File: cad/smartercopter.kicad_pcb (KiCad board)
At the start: 2 copper layers, 37.7 x 16.8 mm, 74 parts, among them P1 CONN_5, P2 CONN_01X01, P3 CONN_01X01, P4 CONN_2, P5 CONN_01X01, P6 CONN_01X01, P7 CONN_01X01, Q1 SiA910EDJ, SW1 SW_PUSH_4, U1 CC2541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

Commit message: everything on board
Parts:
- C1, C2, C3, C6, C7, C8, P1: moved to B.Cu
- moved C25 29.3 mm to (69.7, 119.7), turned to 90 degrees
- moved R11 28.5 mm to (75.0, 120.1), turned to 0 degrees
- moved C27 28.1 mm to (69.6, 118.8), turned to 90 degrees
- moved R18 27.9 mm to (70.8, 119.0), turned to 90 degrees
- moved C21 27.5 mm to (73.6, 119.3), turned to 90 degrees
- moved C17 27.2 mm to (75.5, 119.3), turned to 90 degrees
- moved R19 26.8 mm to (69.7, 117.9), turned to 90 degrees
- moved U4 26.8 mm to (72.1, 118.5), turned to 90 degrees
- moved C18 26.2 mm to (75.1, 118.5), turned to 180 degrees
- moved C23 25.2 mm to (70.2, 116.8), turned to 180 degrees
- moved R15 23.8 mm to (70.2, 115.8), turned to 0 degrees
- moved P1 14.0 mm to (75.3, 107.4), turned to 180 degrees
- moved R16 11.7 mm to (65.1, 108.1)
- moved U3 11.7 mm to (65.6, 108.2)
- moved C20 11.7 mm to (65.1, 109.5)
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
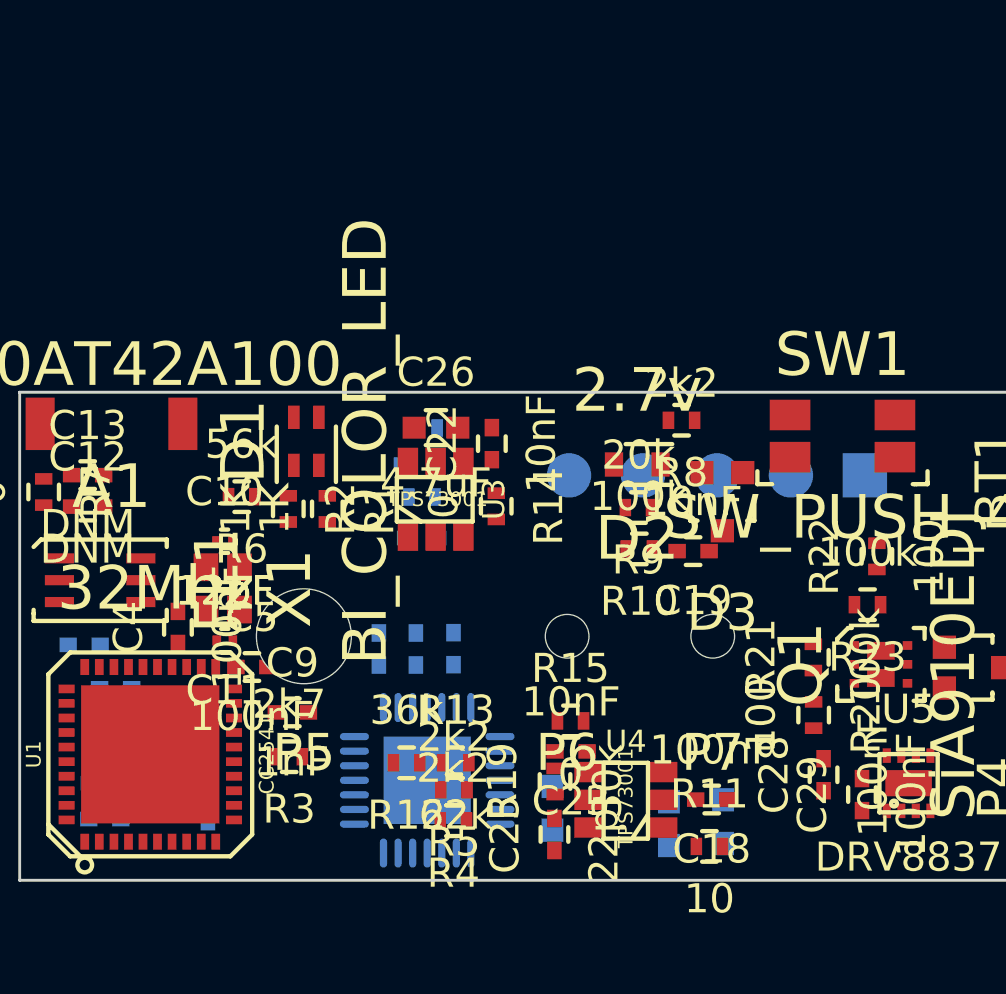
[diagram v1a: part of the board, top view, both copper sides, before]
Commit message: routing first, then placing
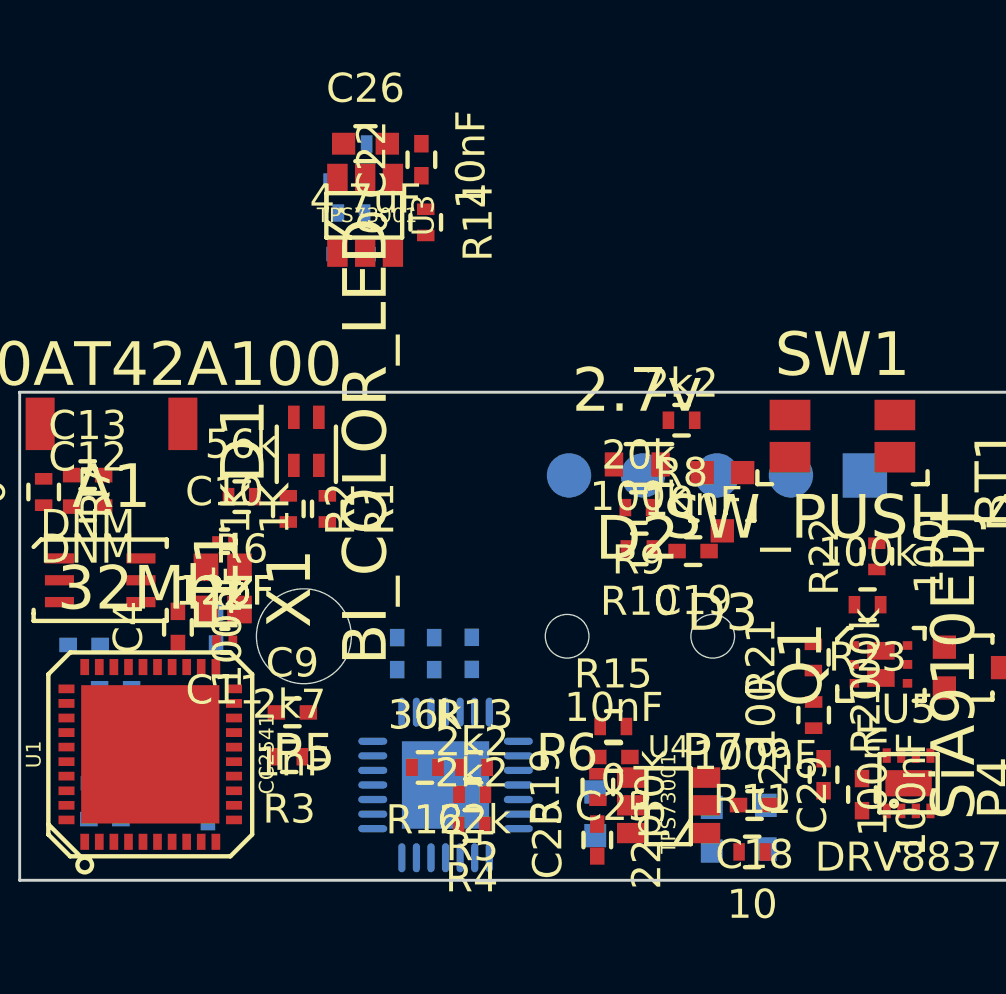
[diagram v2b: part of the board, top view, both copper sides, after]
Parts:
- C5: moved to B.Cu
- moved C20 10.0 mm to (62.7, 99.8)
- moved C22 10.0 mm to (65.1, 96.5)
- moved C24 10.0 mm to (62.6, 97.2)
- moved C26 10.0 mm to (63.2, 96.0)
- moved R14 10.0 mm to (65.3, 98.7)
- moved R16 10.0 mm to (62.7, 98.4)
- moved R17 10.0 mm to (63.7, 96.0)
- moved U3 10.0 mm to (63.2, 98.4)
- moved C5 1.82 mm to (58.1, 112.6), turned to 90 degrees
- moved C23 1.48 mm to (71.7, 117.0)
- moved C17 1.48 mm to (76.9, 119.5)
- moved C18 1.48 mm to (76.5, 118.7)
- moved C21 1.48 mm to (75.1, 119.5)
- moved C25 1.48 mm to (71.2, 119.9)
- moved C27 1.48 mm to (71.1, 119.0)
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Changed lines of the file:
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@@
     (links 168)
     (no_connects 168)
-    (area 39.758145 90.69 93.643934 123.148092)
+    (area 39.758145 101.697 93.643934 123.148092)
     (thickness 1.6)
     (drawings 6)
@@
     )
   )
-  (module Capacitors_SMD:C_0402 (layer F.Cu)
-    (at 59.29 113.95)
-    (descr "Capacitor SMD 0402, reflow soldering, AVX (see smccp.pdf)")
-    (tags "capacitor 0402")
-    (attr smd)
-    (fp_text reference C5 (at 0 -1.7) (layer F.SilkS)
-      (effects (font (size 1 1) (thickness 0.15)))
-    )
-    (fp_text value 100nF (at 0 1.7) (layer F.SilkS)
-      (effects (font (size 1 1) (thickness 0.15)))
-    )
-    (fp_line (start -1.15 -0.6) (end 1.15 -0.6) (layer F.CrtYd) (width 0.05))
-    (fp_line (start -1.15 0.6) (end 1.15 0.6) (layer F.CrtYd) (width 0.05))
-    (fp_line (start -1.15 -0.6) (end -1.15 0.6) (layer F.CrtYd) (width 0.05))
-    (fp_line (start 1.15 -0.6) (end 1.15 0.6) (layer F.CrtYd) (width 0.05))
-    (fp_line (start 0.25 -0.475) (end -0.25 -0.475) (layer F.SilkS) (width 0.15))
-    (fp_line (start -0.25 0.475) (end 0.25 0.475) (layer F.SilkS) (width 0.15))
-    (pad 1 smd rect (at -0.55 0) (size 0.6 0.5) (layers F.Cu F.Paste F.Mask)
-      (net 12 VCCA))
-    (pad 2 smd rect (at 0.55 0) (size 0.6 0.5) (layers F.Cu F.Paste F.Mask)
+  (module Capacitors_SMD:C_0402 (layer B.Cu)
+    (at 58.06 112.61 90)
+    (descr "Capacitor SMD 0402, reflow soldering, AVX (see smccp.pdf)")
+    (tags "capacitor 0402")
+    (attr smd)
+    (fp_text reference C5 (at 0 1.7 90) (layer B.SilkS)
+      (effects (font (size 1 1) (thickness 0.15)) (justify mirror))
+    )
+    (fp_text value 100nF (at 0 -1.7 90) (layer B.SilkS)
+      (effects (font (size 1 1) (thickness 0.15)) (justify mirror))
+    )
+    (fp_line (start -1.15 0.6) (end 1.15 0.6) (layer B.CrtYd) (width 0.05))
+    (fp_line (start -1.15 -0.6) (end 1.15 -0.6) (layer B.CrtYd) (width 0.05))
+    (fp_line (start -1.15 0.6) (end -1.15 -0.6) (layer B.CrtYd) (width 0.05))
+    (fp_line (start 1.15 0.6) (end 1.15 -0.6) (layer B.CrtYd) (width 0.05))
+    (fp_line (start 0.25 0.475) (end -0.25 0.475) (layer B.SilkS) (width 0.15))
+    (fp_line (start -0.25 -0.475) (end 0.25 -0.475) (layer B.SilkS) (width 0.15))
+    (pad 1 smd rect (at -0.55 0 90) (size 0.6 0.5) (layers B.Cu B.Paste B.Mask)
+      (net 12 VCCA))
+    (pad 2 smd rect (at 0.55 0 90) (size 0.6 0.5) (layers B.Cu B.Paste B.Mask)
       (net 5 AGND))
     (model Capacitors_SMD/C_0402E.wrl
@@
   )
   (module Capacitors_SMD:C_0402 (layer B.Cu)
-    (at 64.92 113.33 90)
+    (at 65.55 113.49 90)
     (descr "Capacitor SMD 0402, reflow soldering, AVX (see smccp.pdf)")
     (tags "capacitor 0402")
@@
   )
   (module Capacitors_SMD:C_0402 (layer B.Cu)
-    (at 66.21 113.32 90)
+    (at 66.84 113.48 90)
     (descr "Capacitor SMD 0402, reflow soldering, AVX (see smccp.pdf)")
     (tags "capacitor 0402")
@@
   )
   (module Capacitors_SMD:C_0402 (layer B.Cu)
-    (at 63.65 113.33 90)
+    (at 64.28 113.49 90)
     (descr "Capacitor SMD 0402, reflow soldering, AVX (see smccp.pdf)")
     (tags "capacitor 0402")
@@
   )
   (module Capacitors_SMD:C_0603 (layer B.Cu)
-    (at 75.47 119.26 90)
+    (at 76.94 119.45 90)
     (descr "Capacitor SMD 0603, reflow soldering, AVX (see smccp.pdf)")
     (tags "capacitor 0603")
@@
   )
   (module Capacitors_SMD:C_0402 (layer F.Cu)
-    (at 75.08 118.5 180)
+    (at 76.55 118.69 180)
     (descr "Capacitor SMD 0402, reflow soldering, AVX (see smccp.pdf)")
     (tags "capacitor 0402")
@@
   )
   (module Capacitors_SMD:C_0402 (layer B.Cu)
-    (at 65.12 109.52)
+    (at 62.7 99.77)
     (descr "Capacitor SMD 0402, reflow soldering, AVX (see smccp.pdf)")
     (tags "capacitor 0402")
@@
   )
   (module Capacitors_SMD:C_0603 (layer B.Cu)
-    (at 73.61 119.33 90)
+    (at 75.08 119.52 90)
     (descr "Capacitor SMD 0603, reflow soldering, AVX (see smccp.pdf)")
     (tags "capacitor 0603")
@@
   )
   (module Capacitors_SMD:C_0402 (layer F.Cu)
-    (at 67.53 106.28 90)
+    (at 65.11 96.53 90)
     (descr "Capacitor SMD 0402, reflow soldering, AVX (see smccp.pdf)")
     (tags "capacitor 0402")
@@
   )
   (module Capacitors_SMD:C_0402 (layer F.Cu)
-    (at 70.25 116.85 180)
+    (at 71.72 117.04 180)
     (descr "Capacitor SMD 0402, reflow soldering, AVX (see smccp.pdf)")
     (tags "capacitor 0402")
@@
   )
   (module Capacitors_SMD:C_0402 (layer B.Cu)
-    (at 65.01 107)
+    (at 62.59 97.25)
     (descr "Capacitor SMD 0402, reflow soldering, AVX (see smccp.pdf)")
     (tags "capacitor 0402")
@@
   )
   (module Capacitors_SMD:C_0402 (layer F.Cu)
-    (at 69.68 119.7 90)
+    (at 71.15 119.89 90)
     (descr "Capacitor SMD 0402, reflow soldering, AVX (see smccp.pdf)")
     (tags "capacitor 0402")
@@
   )
   (module Capacitors_SMD:C_0603 (layer F.Cu)
-    (at 65.61 105.73)
+    (at 63.19 95.98)
     (descr "Capacitor SMD 0603, reflow soldering, AVX (see smccp.pdf)")
     (tags "capacitor 0603")
@@
   )
   (module Capacitors_SMD:C_0603 (layer B.Cu)
-    (at 69.61 118.8 90)
+    (at 71.08 118.99 90)
     (descr "Capacitor SMD 0603, reflow soldering, AVX (see smccp.pdf)")
     (tags "capacitor 0603")
@@
   )
   (module Resistors_SMD:R_0402 (layer F.Cu)
-    (at 66.21 119.23 180)
+    (at 66.84 119.39 180)
     (descr "Resistor SMD 0402, reflow soldering, Vishay (see dcrcw.pdf)")
     (tags "resistor 0402")
@@
   )
   (module Resistors_SMD:R_0402 (layer F.Cu)
-    (at 66.228992 118.16156 180)
+    (at 66.858992 118.32156 180)
     (descr "Resistor SMD 0402, reflow soldering, Vishay (see dcrcw.pdf)")
     (tags "resistor 0402")
@@
   )
   (module Resistors_SMD:R_0402 (layer F.Cu)
-    (at 75 120.11)
+    (at 76.47 120.3)
     (descr "Resistor SMD 0402, reflow soldering, Vishay (see dcrcw.pdf)")
     (tags "resistor 0402")
@@
   )
   (module Resistors_SMD:R_0402 (layer F.Cu)
-    (at 64.60159 117.238654 180)
+    (at 65.23159 117.398654 180)
     (descr "Resistor SMD 0402, reflow soldering, Vishay (see dcrcw.pdf)")
     (tags "resistor 0402")
@@
   )
   (module Resistors_SMD:R_0402 (layer F.Cu)
-    (at 66.29 117.23647)
+    (at 66.92 117.39647)
     (descr "Resistor SMD 0402, reflow soldering, Vishay (see dcrcw.pdf)")
     (tags "resistor 0402")
@@
   )
   (module Resistors_SMD:R_0402 (layer F.Cu)
-    (at 67.68 108.43 270)
+    (at 65.26 98.68 270)
     (descr "Resistor SMD 0402, reflow soldering, Vishay (see dcrcw.pdf)")
     (tags "resistor 0402")
@@
   )
   (module Resistors_SMD:R_0402 (layer F.Cu)
-    (at 70.23 115.8)
+    (at 71.7 115.99)
     (descr "Resistor SMD 0402, reflow soldering, Vishay (see dcrcw.pdf)")
     (tags "resistor 0402")
@@
   )
   (module Resistors_SMD:R_0402 (layer B.Cu)
-    (at 65.13 108.11)
+    (at 62.71 98.36)
     (descr "Resistor SMD 0402, reflow soldering, Vishay (see dcrcw.pdf)")
     (tags "resistor 0402")
@@
   )
   (module Resistors_SMD:R_0402 (layer B.Cu)
-    (at 66.1 105.74)
+    (at 63.68 95.99)
     (descr "Resistor SMD 0402, reflow soldering, Vishay (see dcrcw.pdf)")
     (tags "resistor 0402")
@@
   )
   (module Resistors_SMD:R_0402 (layer B.Cu)
-    (at 70.81 119.01 90)
+    (at 72.28 119.2 90)
     (descr "Resistor SMD 0402, reflow soldering, Vishay (see dcrcw.pdf)")
     (tags "resistor 0402")
@@
   )
   (module Resistors_SMD:R_0402 (layer F.Cu)
-    (at 69.7 117.88 90)
+    (at 71.17 118.07 90)
     (descr "Resistor SMD 0402, reflow soldering, Vishay (see dcrcw.pdf)")
     (tags "resistor 0402")
@@
   )
   (module SMD_Packages:QFN-28-1EP (layer B.Cu)
-    (at 65.31 117.84)
+    (at 65.94 118)
     (fp_text reference U2 (at 0 4.20116) (layer B.SilkS)
       (effects (font (size 1.00076 1.00076) (thickness 0.3048)) (justify mirror))
@@
   )
   (module SMD_Packages:SOT-23-6 (layer F.Cu)
-    (at 65.6 108.19)
+    (at 63.18 98.44)
     (fp_text reference U3 (at 1.99898 0 90) (layer F.SilkS)
       (effects (font (size 0.762 0.762) (thickness 0.0762)))
@@
   )
   (module SMD_Packages:SOT-23-6 (layer F.Cu)
-    (at 72.13 118.51 90)
+    (at 73.6 118.7 90)
     (fp_text reference U4 (at 1.99898 0 180) (layer F.SilkS)
       (effects (font (size 0.762 0.762) (thickness 0.0762)))

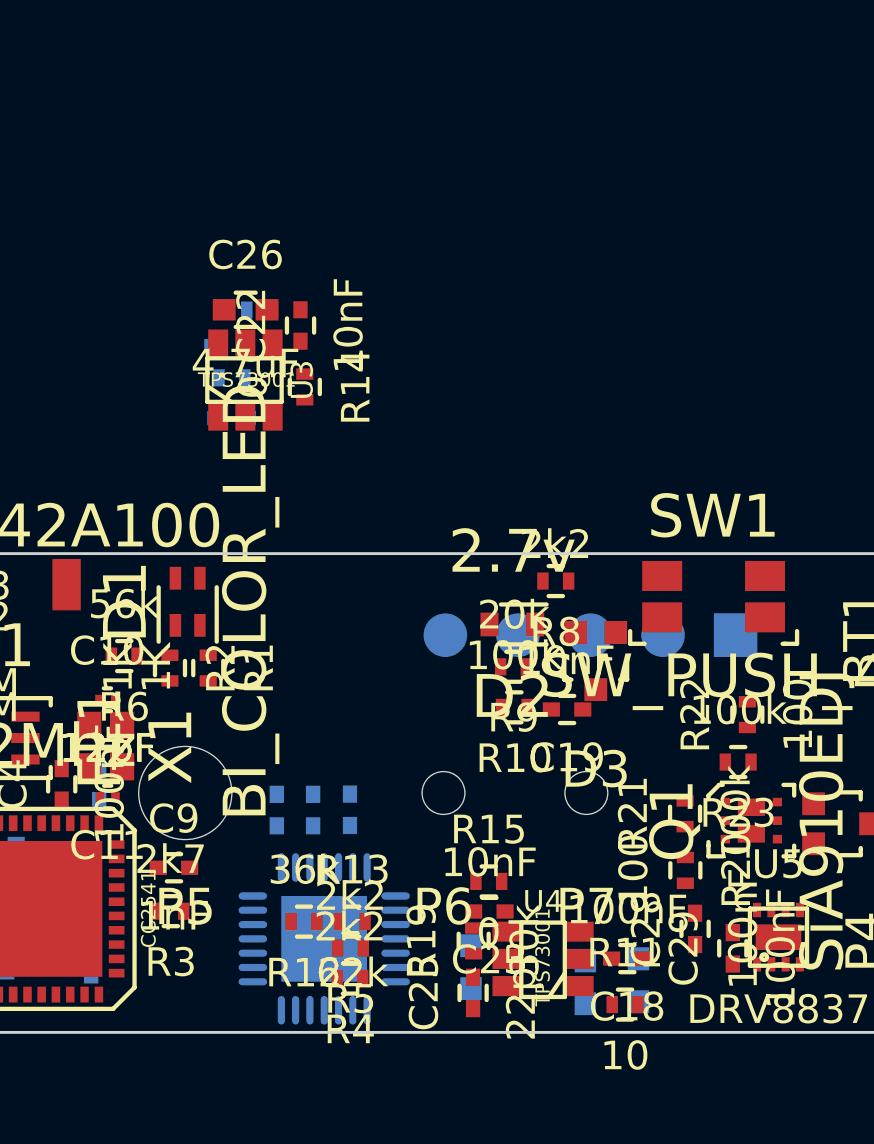
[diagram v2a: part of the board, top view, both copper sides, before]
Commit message: routed voltage regulators
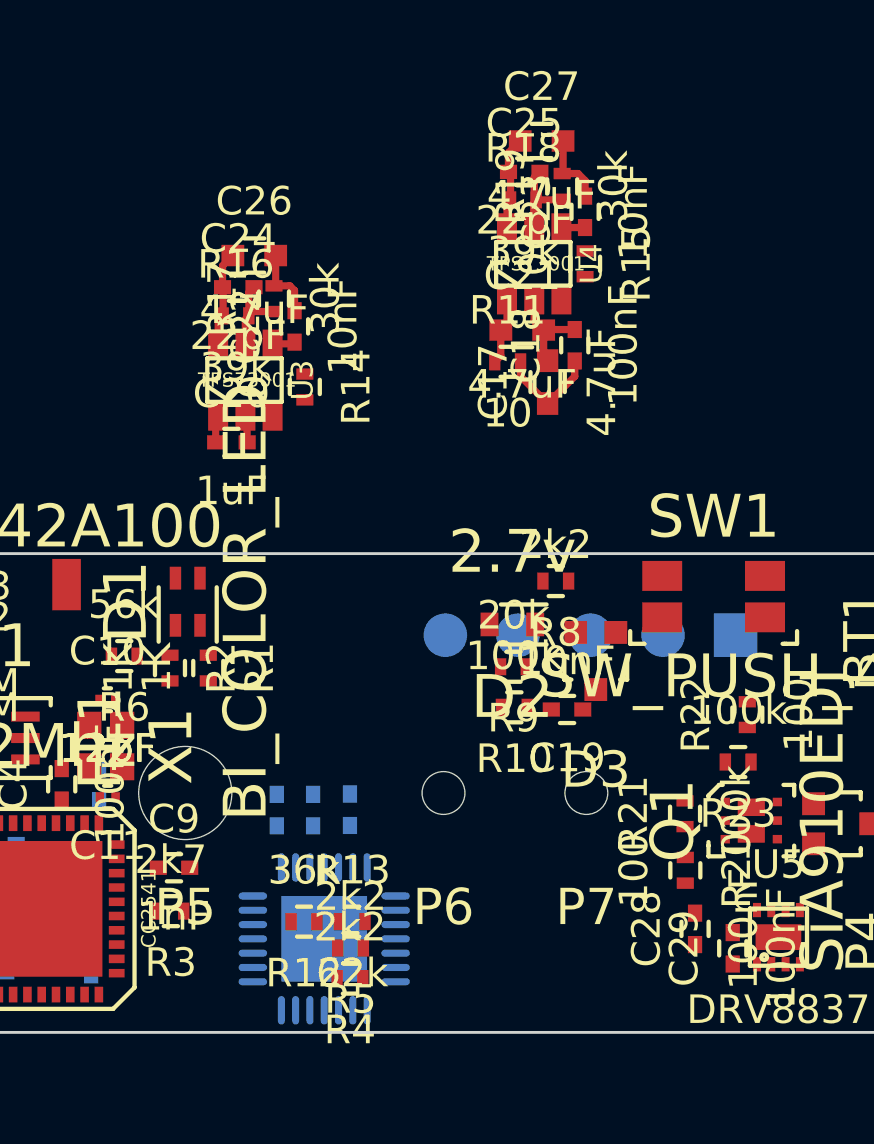
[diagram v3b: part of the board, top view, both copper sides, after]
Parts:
- C17, C20, C21, C24, C27, R16, R17, R18: moved to F.Cu
- moved C27 29.0 mm to (73.5, 90.1), turned to 0 degrees
- moved C25 28.8 mm to (72.9, 91.2), turned to 0 degrees
- moved R18 27.1 mm to (72.9, 92.1), turned to 0 degrees
- moved R19 26.6 mm to (74.3, 91.7)
- moved C23 24.7 mm to (75.1, 92.5), turned to 90 degrees
- moved U4 24.3 mm to (73.3, 94.4), turned to 0 degrees
- moved C21 22.9 mm to (72.9, 96.7), turned to 0 degrees
- moved R11 22.9 mm to (72.4, 97.8)
- moved R15 21.9 mm to (75.1, 94.4), turned to 270 degrees
- moved C18 21.5 mm to (74.7, 97.2), turned to 90 degrees
- moved C17 21.2 mm to (73.8, 98.5)
- moved R16 2.17 mm to (62.9, 96.2)
- moved C24 2.09 mm to (62.9, 95.2)
- moved C26 1.92 mm to (63.5, 94.1)
- moved C20 0.85 mm to (62.7, 100.6)
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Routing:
- net +BATT: track 0.00 -> 4.68 mm
- net GND: track 0.00 -> 4.35 mm
- net Net-(C25-Pad2): track 0.00 -> 3.95 mm
- net VCC: track 0.00 -> 3.32 mm
- net VCCA: track 0.00 -> 3.28 mm
- net Net-(C24-Pad2): track 0.00 -> 3.05 mm
- net AGND: track 0.00 -> 2.60 mm
- net DGND: track 0.00 -> 2.58 mm
- net Net-(C21-Pad1): track 0.00 -> 2.34 mm
- net Net-(C23-Pad1): track 0.00 -> 0.83 mm
- net Net-(C22-Pad1): track 0.00 -> 0.79 mm

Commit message: routed some stuff
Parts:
- C1, C14, C15, C16, C2, C3, C5, C6, C7, C8, U2: moved to F.Cu
- moved C6 41.7 mm to (63.4, 73.9), turned to 90 degrees
- moved C7 40.8 mm to (64.3, 73.9), turned to 90 degrees
- moved C3 40.1 mm to (60.5, 76.2), turned to 180 degrees
- moved C11 39.8 mm to (67.5, 74.3)
- moved C4 39.8 mm to (65.9, 73.9)
- moved X1 39.6 mm to (67.6, 72.7)
- moved U1 39.6 mm to (65.1, 78.5)
- moved C10 39.6 mm to (67.6, 71.2)
- moved C5 39.1 mm to (69.5, 75.2), turned to 0 degrees
- moved C8 39.0 mm to (60.5, 80.6), turned to 180 degrees
- moved C1 38.8 mm to (60.5, 79.7), turned to 180 degrees
- moved C2 37.0 mm to (67.5, 83.0), turned to 270 degrees
- moved U2 36.6 mm to (83.2, 85.7)
- moved R6 34.2 mm to (62.3, 74.1), turned to 270 degrees
- moved R20 33.4 mm to (104.4, 94.4), turned to 180 degrees
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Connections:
- P2 pad 1: Net-(D5-Pad1) -> Net-(D5-Pad2)
- P3 pad 1: Net-(D5-Pad2) -> Net-(D5-Pad1)
- Q1 pad 3: Net-(D5-Pad2) -> Net-(D5-Pad1)
- Q1 pad 6: Net-(D5-Pad1) -> Net-(D5-Pad2)
- Q1 pad D1: Net-(D5-Pad1) -> Net-(D5-Pad2)
- Q1 pad D2: Net-(D5-Pad2) -> Net-(D5-Pad1)
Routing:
- net Net-(D5-Pad2): track 0.00 -> 15.5 mm, vias 0 -> 2
- net GND: track 4.35 -> 14.6 mm, vias 0 -> 2
- net VCCA: track 3.28 -> 11.4 mm
- net Net-(D3-Pad2): track 0.00 -> 7.69 mm
- net Net-(Q1-Pad2): track 0.00 -> 6.68 mm, vias 0 -> 2
- net Net-(D5-Pad1): track 0.00 -> 5.58 mm
- net /XOSC_Q2: track 0.00 -> 4.70 mm
- net AGND: track 2.60 -> 6.56 mm
- net DGND: track 2.58 -> 6.38 mm
- net VCC: track 3.32 -> 6.58 mm
- net +BATT: track 4.68 -> 7.93 mm
- net /XOSC_Q1: track 0.00 -> 2.58 mm
- net /power/BUTTON: track 0.00 -> 2.55 mm
- net Net-(P4-Pad2): track 0.00 -> 2.50 mm
- net Net-(P4-Pad1): track 0.00 -> 2.38 mm
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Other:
- net class Default: clearance 0.254 -> 0.0508; via_dia 0.889 -> 0.762; via_drill 0.635 -> 0.508
- rule trace_clearance: 0.254 -> 0.0508
- rule via_min_size: 0.889 -> 0.762

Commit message: stuff on board with a bit of routing
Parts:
- C1, C14, C15, C16, C2, C3, C4, C5, C6, C7, C8: moved to B.Cu
- moved C4 42.2 mm to (56.2, 115.0), turned to 270 degrees
- moved R6 40.6 mm to (51.9, 113.3)
- moved C5 40.3 mm to (57.4, 113.6), turned to 270 degrees
- moved C6 39.8 mm to (52.5, 112.2), turned to 180 degrees
- moved D1 39.4 mm to (46.6, 115.6)
- moved R1 39.4 mm to (48.9, 114.9)
- moved R2 39.4 mm to (48.9, 116.2)
- moved U1 39.4 mm to (55.6, 116.7)
- moved C7 39.2 mm to (52.5, 111.3), turned to 180 degrees
- moved C3 39.2 mm to (53.9, 114.9), turned to 0 degrees
- moved C8 39.0 mm to (53.1, 118.9), turned to 0 degrees
- moved C1 38.8 mm to (53.2, 117.8), turned to 0 degrees
- moved C11 38.6 mm to (58.9, 111.9)
- moved C10 38.6 mm to (59.0, 108.8)
- moved X1 38.6 mm to (59.0, 110.3)
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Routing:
- net /sensors/SCL: track 0.00 -> 10.7 mm
- net /sensors/SDA: track 0.00 -> 10.1 mm, vias 0 -> 2
- net VCCA: track 11.4 -> 6.07 mm
- net AGND: track 6.56 -> 2.60 mm
- net /XOSC_Q2: track 4.70 -> 0.94 mm
- net /XOSC_Q1: track 2.58 -> 0.00 mm
- net VCC: track 6.58 -> 4.15 mm
- net /RF_N: track 0.00 -> 2.32 mm
- net /RF_P: track 0.00 -> 2.28 mm
- net Net-(C14-Pad1): track 1.41 -> 0.18 mm
- net Net-(C8-Pad1): track 1.23 -> 0.00 mm
- net Net-(R6-Pad2): track 1.19 -> 0.00 mm
- net DGND: track 6.38 -> 5.79 mm
